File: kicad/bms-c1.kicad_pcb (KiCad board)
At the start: 4 copper layers, 135 x 70 mm, 209 parts, among them J1 MicroFit 2x12, J2 B4B-PH-SM4, J3 USB_C_Receptacle_USB2.0, J4 B3B-PH-SM4, J5 B2B-PH-SM4, J6 B4B-PH-SM4, P1 CONN_01X01, P2 CONN_01X01, P3 CONN_01X01, P4 CONN_01X01, P5 CONN_01X01, Q1 DMN10H220LE, Q10 BSS84, Q11 BSS123N, Q12 ZXMP10A17GTA, Q2 IPT012N08N5, Q3 IPT012N08N5, Q4 IPT012N08N5, Q5 IPT012N08N5, Q6 IPT012N08N5, Q7 IPT012N08N5, Q8 IPT012N08N5, Q9 IPT012N08N5, U1 SN65HVD230, U2 SN65HVD75, U3 LMR38010, U4 BQ76952, U5 ESP32-C3-MINI-1

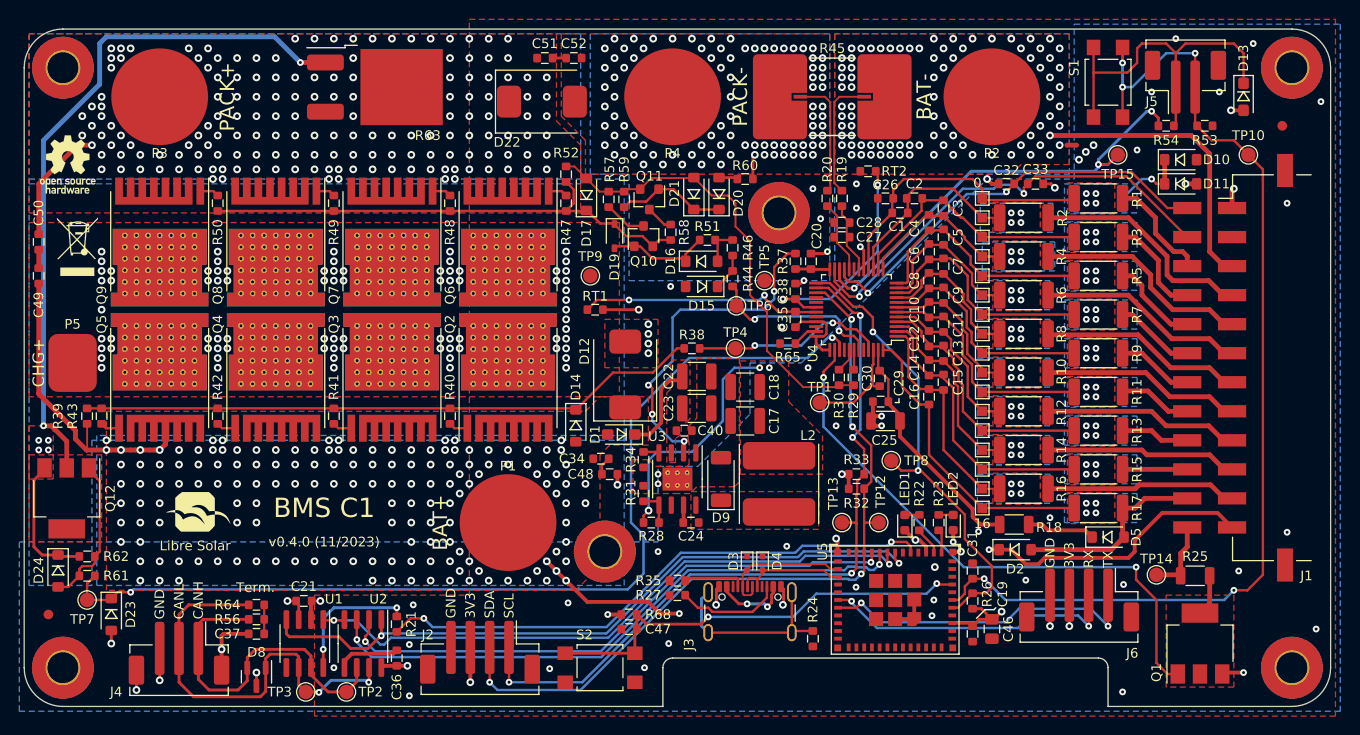
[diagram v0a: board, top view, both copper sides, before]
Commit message: Increase clearance around NPTH (v0.4.1)
The NPTHs of the USB connector are very close to the pads, such that a
clearance of 0.25 mm as required by some manufacturers was not possible.
The clearance is now 0.2 mm.

Fixes #55
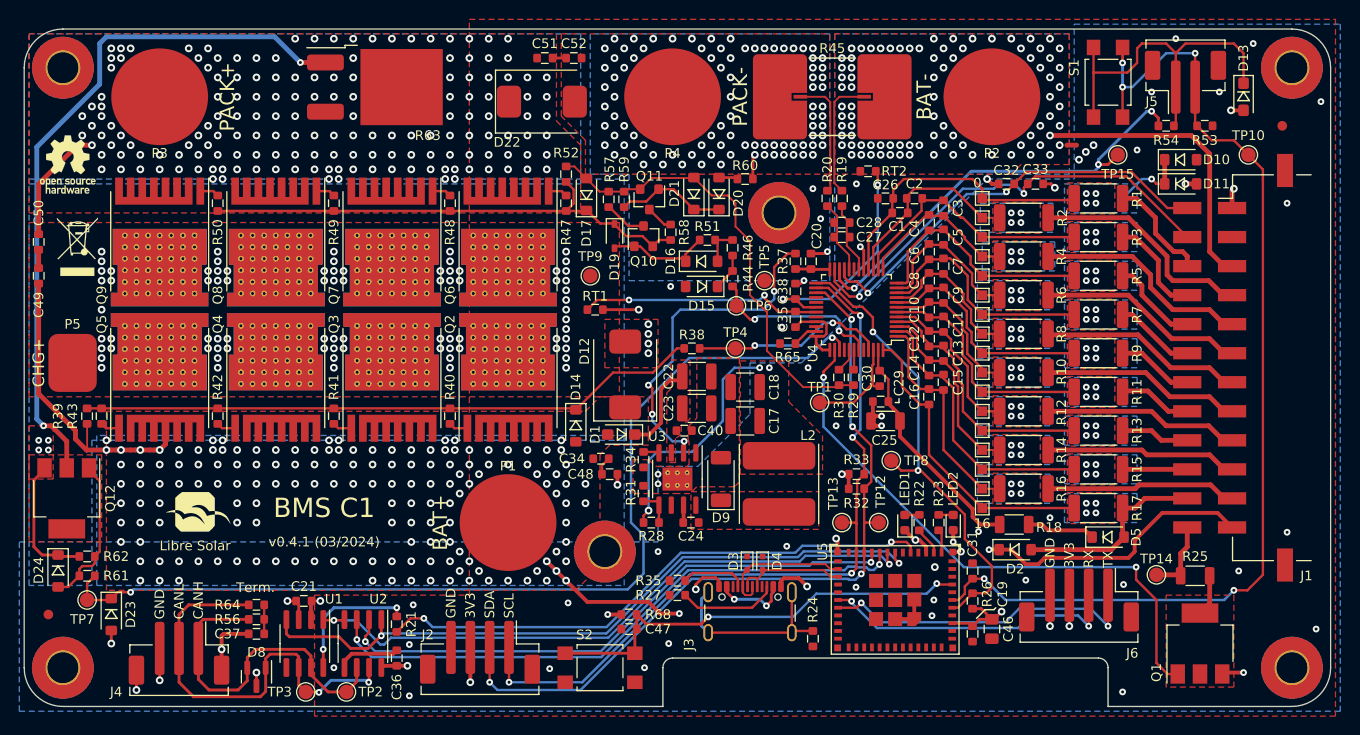
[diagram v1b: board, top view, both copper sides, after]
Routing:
- net GND: track 72.3 -> 76.0 mm
- net Net-(J3-CC2): track 10.9 -> 10.3 mm
- net Net-(Q12-D): track 72.4 -> 73.0 mm
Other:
- board text added: "v0.4.1 (03/2024)"
- board text removed: "v0.4.0 (11/2023)"

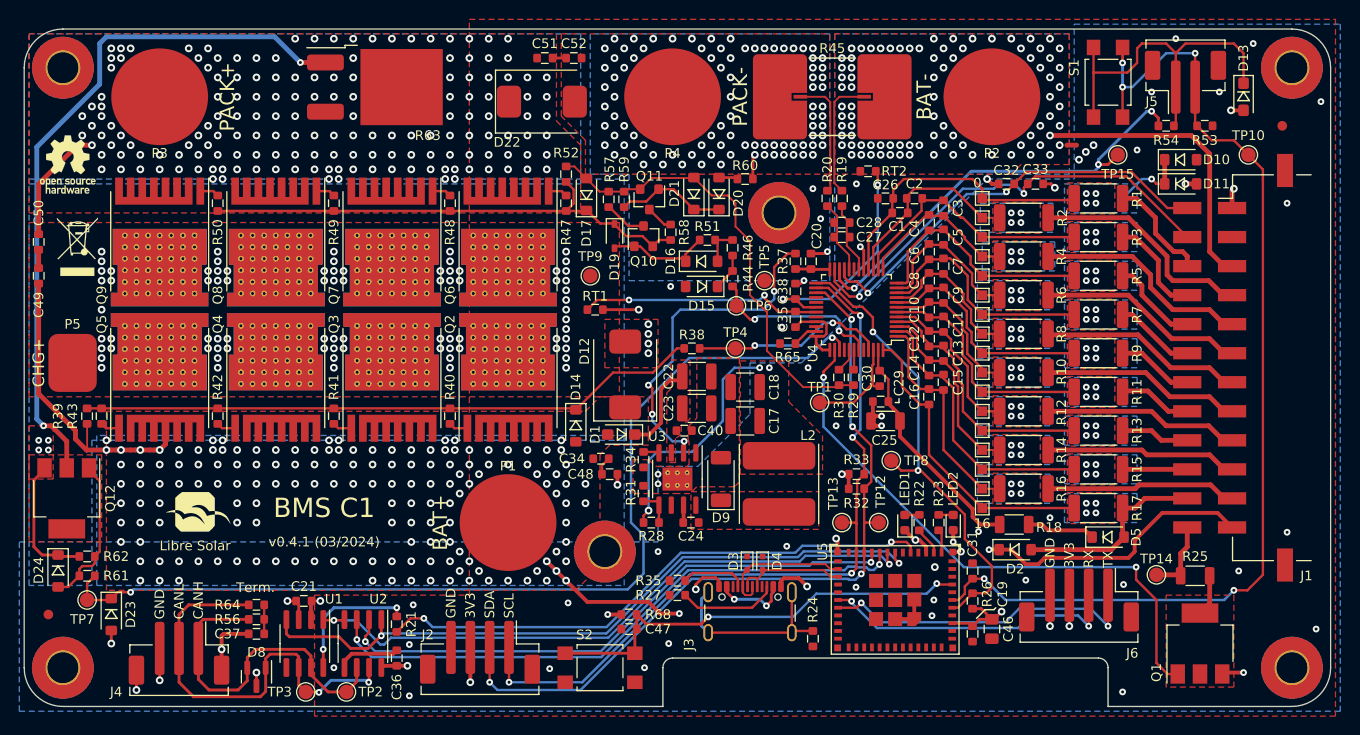
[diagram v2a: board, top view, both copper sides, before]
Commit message: Create cost-optimized Lite variant of the BMS C1 v0.4.1
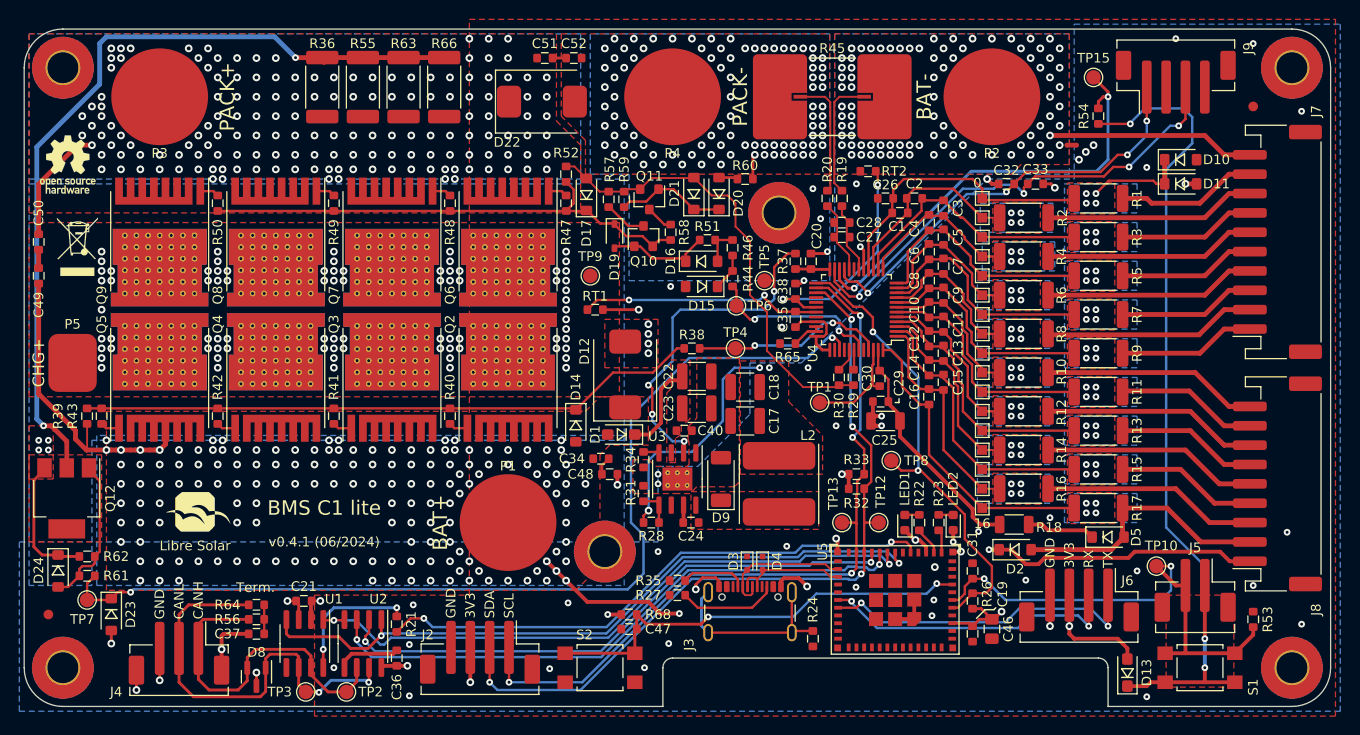
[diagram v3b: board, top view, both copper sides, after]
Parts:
- removed J1: MicroFit 2x12, Connector_Molex:Molex_Micro-Fit_3.0_43045-2410_2x12-1MP_P3.00mm_Horizontal
- removed Q1: DMN10H220LE, Package_TO_SOT_SMD:SOT-223
- removed R25: 10, LibreSolar:R_1206_3216
- removed TP14: TestPoint, TestPoint:TestPoint_Pad_D1.5mm
- added J7: Conn_01x10_MountingPin, Connector_JST:JST_PH_S10B-PH-SM4-TB_1x10-1MP_P2.00mm_Horizontal, F.Cu at (209.5, 72.0)
- added J8: Conn_01x10_MountingPin, Connector_JST:JST_PH_S9B-PH-SM4-TB_1x09-1MP_P2.00mm_Horizontal, F.Cu at (209.5, 97.0)
- added J9: B4B-PH-SM4, Connector_JST:JST_PH_B4B-PH-SM4-TB_1x04-1MP_P2.00mm_Vertical, F.Cu at (199.0, 55.5)
- added R36: 180, Resistor_SMD:R_2512_6332Metric_Pad1.40x3.35mm_HandSolder, F.Cu at (110.8, 56.0)
- added R55: 180, Resistor_SMD:R_2512_6332Metric_Pad1.40x3.35mm_HandSolder, F.Cu at (115.0, 56.0)
- added R66: 180, Resistor_SMD:R_2512_6332Metric_Pad1.40x3.35mm_HandSolder, F.Cu at (123.4, 56.0)
- R63: value 40 -> 180; footprint LibreSolar:Bourns_PWR163 -> Resistor_SMD:R_2512_6332Metric_Pad1.40x3.35mm_HandSolder
- moved S1 61.2 mm to (201.5, 116.0), turned to 0 degrees
- moved D13 60.7 mm to (194.0, 116.5), turned to 90 degrees
- moved J5 52.5 mm to (201.0, 108.0), turned to 180 degrees
- moved R53 51.2 mm to (207.0, 111.0), turned to -90 degrees
- moved TP10 43.5 mm to (197.0, 105.5)
- moved TP15 8.38 mm to (190.5, 55.0), turned to 180 degrees
- moved R54 7.07 mm to (191.0, 59.0), turned to 90 degrees
- moved FID2 3.61 mm to (207.0, 58.0)
- moved R63 2.99 mm to (119.2, 56.0), turned to 90 degrees
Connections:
- J3 pad A9: unconnected-(J3-VBUS-PadA4) -> unconnected-(J3-VBUS-PadA4)_2
- J3 pad B4: unconnected-(J3-VBUS-PadA4) -> unconnected-(J3-VBUS-PadA4)_1
- J3 pad B9: unconnected-(J3-VBUS-PadA4) -> unconnected-(J3-VBUS-PadA4)_0
- R63 pad 1: Net-(Q12-D) -> /PACK+
- R63 pad 2: /PACK+ -> Net-(Q12-D)
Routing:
- net +3V3: track 121.2 -> 57.6 mm, vias 11 -> 10
- net Net-(U4-FUSE): track 60.2 -> 0.00 mm, vias 2 -> 0
- net /BTN_LOW: track 109.7 -> 50.8 mm, vias 5 -> 2
- net /BQ76952/BTN_HIGH: track 36.7 -> 88.7 mm, vias 0 -> 3
- net Net-(Q12-D): track 73.0 -> 85.1 mm
- net /BAT-: track 31.4 -> 22.6 mm
- net /C14+: track 6.69 -> 14.6 mm
- net /FUSE: track 7.83 -> 0.00 mm
- net unconnected-(J3-VBUS-PadA4): track 7.53 -> 0.00 mm, vias 2 -> 0
- net /C12+: track 7.10 -> 14.6 mm
- net /C16+: track 20.3 -> 27.8 mm
- net /C10+: track 7.55 -> 14.6 mm
- net /C8+: track 7.93 -> 14.2 mm
- net /C6+: track 8.34 -> 14.2 mm
- net /C4+: track 9.34 -> 14.2 mm
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- added copper zone on F.Cu, net (none)
- removed copper zone on F.Cu, net Net-(Q1-D-Pad2)
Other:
- board text added: "BMS C1 lite"
- board text added: "v0.4.1 (06/2024)"
- board text removed: "BMS C1"
- board text removed: "v0.4.1 (03/2024)"
